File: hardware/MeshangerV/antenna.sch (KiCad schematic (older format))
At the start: 4 parts

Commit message: schematic complete more or less
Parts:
- removed AE?: Antenna_Dipole, symbol Device:Antenna_Dipole
- added J?: Conn_Coaxial, symbol Connector:Conn_Coaxial
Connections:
- wire segments 0 -> 11
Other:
- moved on the sheet: C?, L?
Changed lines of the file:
@@
 EESchema Schematic File Version 4
 LIBS:MeshangerV-cache
-EELAYER 26 0
+EELAYER 29 0
 EELAYER END
 $Descr A4 11693 8268
 encoding utf-8
-Sheet 4 4
+Sheet 4 5
 Title ""
 Date ""
@@
 L Device:L_Small L?
 U 1 1 5FC5BF06
-P 2950 2850
-F 0 "L?" H 2997 2896 50  0000 L CNN
-F 1 "L_Small" H 2997 2805 50  0000 L CNN
-F 2 "" H 2950 2850 50  0001 C CNN
-F 3 "~" H 2950 2850 50  0001 C CNN
-	1    2950 2850
-	1    0    0    -1
+P 4400 3200
+F 0 "L?" H 4447 3246 50  0000 L CNN
+F 1 "L_Small" H 4447 3155 50  0000 L CNN
+F 2 "" H 4400 3200 50  0001 C CNN
+F 3 "~" H 4400 3200 50  0001 C CNN
+	1    4400 3200
+	0    -1   -1   0
 $EndComp
 $Comp
 L Device:C_Small C?
 U 1 1 5FC5BFAB
-P 3700 3500
-F 0 "C?" H 3792 3546 50  0000 L CNN
-F 1 "C_Small" H 3792 3455 50  0000 L CNN
-F 2 "" H 3700 3500 50  0001 C CNN
-F 3 "~" H 3700 3500 50  0001 C CNN
-	1    3700 3500
+P 4950 3550
+F 0 "C?" H 5042 3596 50  0000 L CNN
+F 1 "C_Small" H 5042 3505 50  0000 L CNN
+F 2 "" H 4950 3550 50  0001 C CNN
+F 3 "~" H 4950 3550 50  0001 C CNN
+	1    4950 3550
 	1    0    0    -1
 $EndComp
@@
 L Device:C_Small C?
 U 1 1 5FC5C01F
-P 2950 4200
-F 0 "C?" H 3042 4246 50  0000 L CNN
-F 1 "C_Small" H 3042 4155 50  0000 L CNN
-F 2 "" H 2950 4200 50  0001 C CNN
-F 3 "~" H 2950 4200 50  0001 C CNN
-	1    2950 4200
+P 3750 3550
+F 0 "C?" H 3842 3596 50  0000 L CNN
+F 1 "C_Small" H 3842 3505 50  0000 L CNN
+F 2 "" H 3750 3550 50  0001 C CNN
+F 3 "~" H 3750 3550 50  0001 C CNN
+	1    3750 3550
 	1    0    0    -1
 $EndComp
+Wire Wire Line
+	3750 3450 3750 3200
+Wire Wire Line
+	3750 3200 4300 3200
+Wire Wire Line
+	4500 3200 4950 3200
+Wire Wire Line
+	4950 3200 4950 3450
+Wire Wire Line
+	3750 3650 3750 4100
+Wire Wire Line
+	4950 3650 4950 4100
 $Comp
-L Device:Antenna_Dipole AE?
-U 1 1 5FC5C11F
-P 4200 2250
-F 0 "AE?" H 4430 2166 50  0000 L CNN
-F 1 "Antenna_Dipole" H 4430 2075 50  0000 L CNN
-F 2 "" H 4200 2250 50  0001 C CNN
-F 3 "~" H 4200 2250 50  0001 C CNN
-	1    4200 2250
+L Connector:Conn_Coaxial J?
+U 1 1 5FC624A8
+P 5500 3200
+F 0 "J?" H 5600 3175 50  0000 L CNN
+F 1 "Conn_Coaxial" H 5600 3084 50  0000 L CNN
+F 2 "" H 5500 3200 50  0001 C CNN
+F 3 " ~" H 5500 3200 50  0001 C CNN
+	1    5500 3200
 	1    0    0    -1
 $EndComp
+Wire Wire Line
+	5300 3200 4950 3200
+Connection ~ 4950 3200
+Wire Wire Line
+	5500 3400 5500 4100
+Wire Wire Line
+	3750 3200 3300 3200
+Connection ~ 3750 3200
+Text Label 3300 3200 0    50   ~ 0
+ANT
+Text Label 3750 4100 0    50   ~ 0
+GND
+Text Label 3050 1050 0    50   ~ 0
+GND
+Text Label 2250 1050 0    50   ~ 0
+ANT
+Text Label 4950 4100 0    50   ~ 0
+GND
+Text Label 5500 4100 0    50   ~ 0
+GND
+Wire Wire Line
+	2000 1050 2250 1050
+Wire Wire Line
+	2800 1050 3050 1050
 $EndSCHEMATC

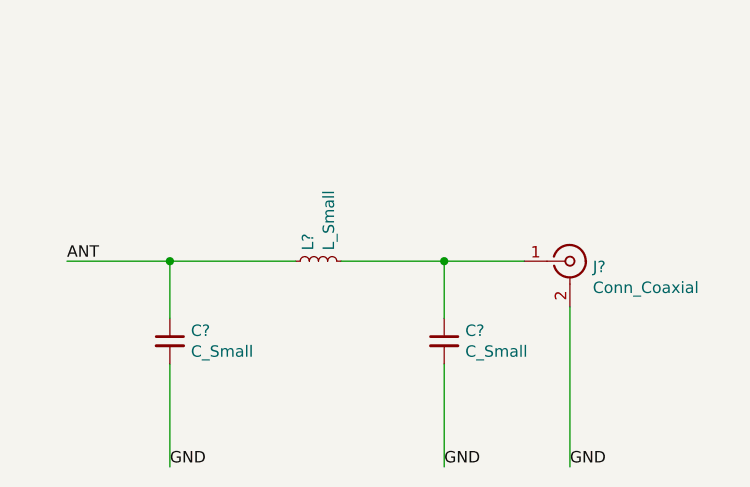
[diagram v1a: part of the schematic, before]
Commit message: routing has begun
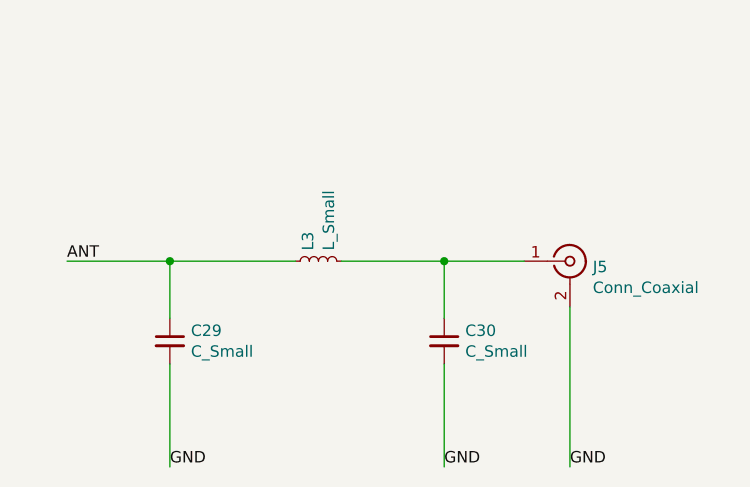
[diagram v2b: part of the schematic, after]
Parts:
- C29, C30: renamed from C?; footprint (none) -> Capacitor_SMD:C_0603_1608Metric
- J5: renamed from J?; footprint (none) -> Connector_Coaxial:SMA_Samtec_SMA-J-P-H-ST-EM1_EdgeMount
- L3: renamed from L?; footprint (none) -> Inductors_SMD:L_0805
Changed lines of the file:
@@
 EESchema Schematic File Version 4
 LIBS:MeshangerV-cache
-EELAYER 29 0
+EELAYER 26 0
 EELAYER END
 $Descr A4 11693 8268
@@
 VCC
 $Comp
-L Device:L_Small L?
+L Device:L_Small L3
 U 1 1 5FC5BF06
 P 4400 3200
-F 0 "L?" H 4447 3246 50  0000 L CNN
+F 0 "L3" H 4447 3246 50  0000 L CNN
 F 1 "L_Small" H 4447 3155 50  0000 L CNN
-F 2 "" H 4400 3200 50  0001 C CNN
+F 2 "Inductors_SMD:L_0805" H 4400 3200 50  0001 C CNN
 F 3 "~" H 4400 3200 50  0001 C CNN
 	1    4400 3200
@@
 $EndComp
 $Comp
-L Device:C_Small C?
+L Device:C_Small C30
 U 1 1 5FC5BFAB
 P 4950 3550
-F 0 "C?" H 5042 3596 50  0000 L CNN
+F 0 "C30" H 5042 3596 50  0000 L CNN
 F 1 "C_Small" H 5042 3505 50  0000 L CNN
-F 2 "" H 4950 3550 50  0001 C CNN
+F 2 "Capacitor_SMD:C_0603_1608Metric" H 4950 3550 50  0001 C CNN
 F 3 "~" H 4950 3550 50  0001 C CNN
 	1    4950 3550
@@
 $EndComp
 $Comp
-L Device:C_Small C?
+L Device:C_Small C29
 U 1 1 5FC5C01F
 P 3750 3550
-F 0 "C?" H 3842 3596 50  0000 L CNN
+F 0 "C29" H 3842 3596 50  0000 L CNN
 F 1 "C_Small" H 3842 3505 50  0000 L CNN
-F 2 "" H 3750 3550 50  0001 C CNN
+F 2 "Capacitor_SMD:C_0603_1608Metric" H 3750 3550 50  0001 C CNN
 F 3 "~" H 3750 3550 50  0001 C CNN
 	1    3750 3550
@@
 	4950 3650 4950 4100
 $Comp
-L Connector:Conn_Coaxial J?
+L Connector:Conn_Coaxial J5
 U 1 1 5FC624A8
 P 5500 3200
-F 0 "J?" H 5600 3175 50  0000 L CNN
+F 0 "J5" H 5600 3175 50  0000 L CNN
 F 1 "Conn_Coaxial" H 5600 3084 50  0000 L CNN
-F 2 "" H 5500 3200 50  0001 C CNN
+F 2 "Connector_Coaxial:SMA_Samtec_SMA-J-P-H-ST-EM1_EdgeMount" H 5500 3200 50  0001 C CNN
 F 3 " ~" H 5500 3200 50  0001 C CNN
 	1    5500 3200
